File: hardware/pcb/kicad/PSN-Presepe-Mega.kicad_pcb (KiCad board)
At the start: 2 copper layers, 280 x 170 mm, 83 parts, among them J1 12V_IN, K1 G5Q-1_DC12, K10 G5Q-1_DC12, K11 G5Q-1_DC12, K12 G5Q-1_DC12, K13 G5Q-1_DC12, K14 G5Q-1_DC12, K15 G5Q-1_DC12, K16 G5Q-1_DC12, K2 G5Q-1_DC12, K3 G5Q-1_DC12, K4 G5Q-1_DC12, K5 G5Q-1_DC12, K6 G5Q-1_DC12, K7 G5Q-1_DC12, K8 G5Q-1_DC12, K9 G5Q-1_DC12, Q1 IRLZ44N_CIELO_R, Q2 IRLZ44N_CIELO_G, Q3 IRLZ44N_CIELO_B, Q4 IRLZ44N_TRAM_R, Q5 IRLZ44N_TRAM_G, Q6 IRLZ44N_TRAM_B, Q7 IRLZ44N_ALBA_R, Q8 IRLZ44N_ALBA_G, Q9 IRLZ44N_ALBA_B, U1 ULN2803C, U2 ULN2803C

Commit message: Promote KiCad-validated K4 coil route
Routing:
- net RELAY4_COIL_LOW: track 0.00 -> 76.4 mm
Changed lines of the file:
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@@
   (segment (start 191 69) (end 193.62 64) (width 0.3) (layer "F.Cu") (net 38))
   (segment (start 193.62 64) (end 193.62 60) (width 0.3) (layer "F.Cu") (net 38))
+  (segment (start 145.16 69.62) (end 148.0 71.5) (width 0.3) (layer "F.Cu") (net 39))
+  (segment (start 148.0 71.5) (end 209.0 71.5) (width 0.3) (layer "F.Cu") (net 39))
+  (segment (start 209.0 71.5) (end 211.62 64.0) (width 0.3) (layer "F.Cu") (net 39))
+  (segment (start 211.62 64.0) (end 211.62 60.0) (width 0.3) (layer "F.Cu") (net 39))
   (gr_rect (start 20 20) (end 300 190) (stroke (width 0.5) (type default)) (fill none) (layer "Edge.Cuts"))
   (gr_rect (start 53 128) (end 118 172) (stroke (width 0.3) (type dash)) (fill none) (layer "Dwgs.User"))

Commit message: Promote KiCad-validated K5 coil route
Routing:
- net RELAY5_COIL_LOW: track 0.00 -> 96.7 mm
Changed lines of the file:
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@@
   (segment (start 209.0 71.5) (end 211.62 64.0) (width 0.3) (layer "F.Cu") (net 39))
   (segment (start 211.62 64.0) (end 211.62 60.0) (width 0.3) (layer "F.Cu") (net 39))
+  (segment (start 145.16 72.16) (end 148 74) (width 0.3) (layer "F.Cu") (net 40))
+  (segment (start 148 74) (end 227 74) (width 0.3) (layer "F.Cu") (net 40))
+  (segment (start 227 74) (end 229.62 64) (width 0.3) (layer "F.Cu") (net 40))
+  (segment (start 229.62 64) (end 229.62 60) (width 0.3) (layer "F.Cu") (net 40))
   (gr_rect (start 20 20) (end 300 190) (stroke (width 0.5) (type default)) (fill none) (layer "Edge.Cuts"))
   (gr_rect (start 53 128) (end 118 172) (stroke (width 0.3) (type dash)) (fill none) (layer "Dwgs.User"))

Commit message: Promote KiCad-validated K6 coil route
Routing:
- net RELAY6_COIL_LOW: track 0.00 -> 117.1 mm
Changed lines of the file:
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@@
   (segment (start 227 74) (end 229.62 64) (width 0.3) (layer "F.Cu") (net 40))
   (segment (start 229.62 64) (end 229.62 60) (width 0.3) (layer "F.Cu") (net 40))
+  (segment (start 145.16 74.7) (end 148 76.5) (width 0.3) (layer "F.Cu") (net 41))
+  (segment (start 148 76.5) (end 245 76.5) (width 0.3) (layer "F.Cu") (net 41))
+  (segment (start 245 76.5) (end 247.62 64) (width 0.3) (layer "F.Cu") (net 41))
+  (segment (start 247.62 64) (end 247.62 60) (width 0.3) (layer "F.Cu") (net 41))
   (gr_rect (start 20 20) (end 300 190) (stroke (width 0.5) (type default)) (fill none) (layer "Edge.Cuts"))
   (gr_rect (start 53 128) (end 118 172) (stroke (width 0.3) (type dash)) (fill none) (layer "Dwgs.User"))

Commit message: Promote KiCad-validated K7 coil route
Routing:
- net RELAY7_COIL_LOW: track 0.00 -> 137.6 mm
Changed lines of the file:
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@@
   (segment (start 245 76.5) (end 247.62 64) (width 0.3) (layer "F.Cu") (net 41))
   (segment (start 247.62 64) (end 247.62 60) (width 0.3) (layer "F.Cu") (net 41))
+  (segment (start 145.16 77.24) (end 148 79) (width 0.3) (layer "F.Cu") (net 42))
+  (segment (start 148 79) (end 263 79) (width 0.3) (layer "F.Cu") (net 42))
+  (segment (start 263 79) (end 265.62 64) (width 0.3) (layer "F.Cu") (net 42))
+  (segment (start 265.62 64) (end 265.62 60) (width 0.3) (layer "F.Cu") (net 42))
   (gr_rect (start 20 20) (end 300 190) (stroke (width 0.5) (type default)) (fill none) (layer "Edge.Cuts"))
   (gr_rect (start 53 128) (end 118 172) (stroke (width 0.3) (type dash)) (fill none) (layer "Dwgs.User"))

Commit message: Promote KiCad-validated K8 coil route
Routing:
- net RELAY8_COIL_LOW: track 0.00 -> 158.0 mm
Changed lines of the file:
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@@
   (segment (start 263 79) (end 265.62 64) (width 0.3) (layer "F.Cu") (net 42))
   (segment (start 265.62 64) (end 265.62 60) (width 0.3) (layer "F.Cu") (net 42))
+  (segment (start 145.16 79.78) (end 148 81.5) (width 0.3) (layer "F.Cu") (net 43))
+  (segment (start 148 81.5) (end 281 81.5) (width 0.3) (layer "F.Cu") (net 43))
+  (segment (start 281 81.5) (end 283.62 64) (width 0.3) (layer "F.Cu") (net 43))
+  (segment (start 283.62 64) (end 283.62 60) (width 0.3) (layer "F.Cu") (net 43))
   (gr_rect (start 20 20) (end 300 190) (stroke (width 0.5) (type default)) (fill none) (layer "Edge.Cuts"))
   (gr_rect (start 53 128) (end 118 172) (stroke (width 0.3) (type dash)) (fill none) (layer "Dwgs.User"))

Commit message: Promote KiCad-validated K9 coil route
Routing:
- net RELAY9_COIL_LOW: track 0.00 -> 34.2 mm
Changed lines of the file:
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@@
   (segment (start 281 81.5) (end 283.62 64) (width 0.3) (layer "F.Cu") (net 43))
   (segment (start 283.62 64) (end 283.62 60) (width 0.3) (layer "F.Cu") (net 43))
+  (segment (start 145.16 92) (end 147.5 94) (width 0.3) (layer "F.Cu") (net 44))
+  (segment (start 147.5 94) (end 147.5 112) (width 0.3) (layer "F.Cu") (net 44))
+  (segment (start 147.5 112) (end 157.62 112) (width 0.3) (layer "F.Cu") (net 44))
+  (segment (start 157.62 112) (end 157.62 115) (width 0.3) (layer "F.Cu") (net 44))
   (gr_rect (start 20 20) (end 300 190) (stroke (width 0.5) (type default)) (fill none) (layer "Edge.Cuts"))
   (gr_rect (start 53 128) (end 118 172) (stroke (width 0.3) (type dash)) (fill none) (layer "Dwgs.User"))

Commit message: Promote KiCad-validated K10 coil route
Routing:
- net RELAY10_COIL_LOW: track 0.00 -> 61.8 mm
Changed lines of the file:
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@@
   (segment (start 147.5 112) (end 157.62 112) (width 0.3) (layer "F.Cu") (net 44))
   (segment (start 157.62 112) (end 157.62 115) (width 0.3) (layer "F.Cu") (net 44))
+  (segment (start 145.16 94.54) (end 142 96.5) (width 0.3) (layer "F.Cu") (net 45))
+  (segment (start 142 96.5) (end 142 118) (width 0.3) (layer "F.Cu") (net 45))
+  (segment (start 142 118) (end 175.62 118) (width 0.3) (layer "F.Cu") (net 45))
+  (segment (start 175.62 118) (end 175.62 115) (width 0.3) (layer "F.Cu") (net 45))
   (gr_rect (start 20 20) (end 300 190) (stroke (width 0.5) (type default)) (fill none) (layer "Edge.Cuts"))
   (gr_rect (start 53 128) (end 118 172) (stroke (width 0.3) (type dash)) (fill none) (layer "Dwgs.User"))

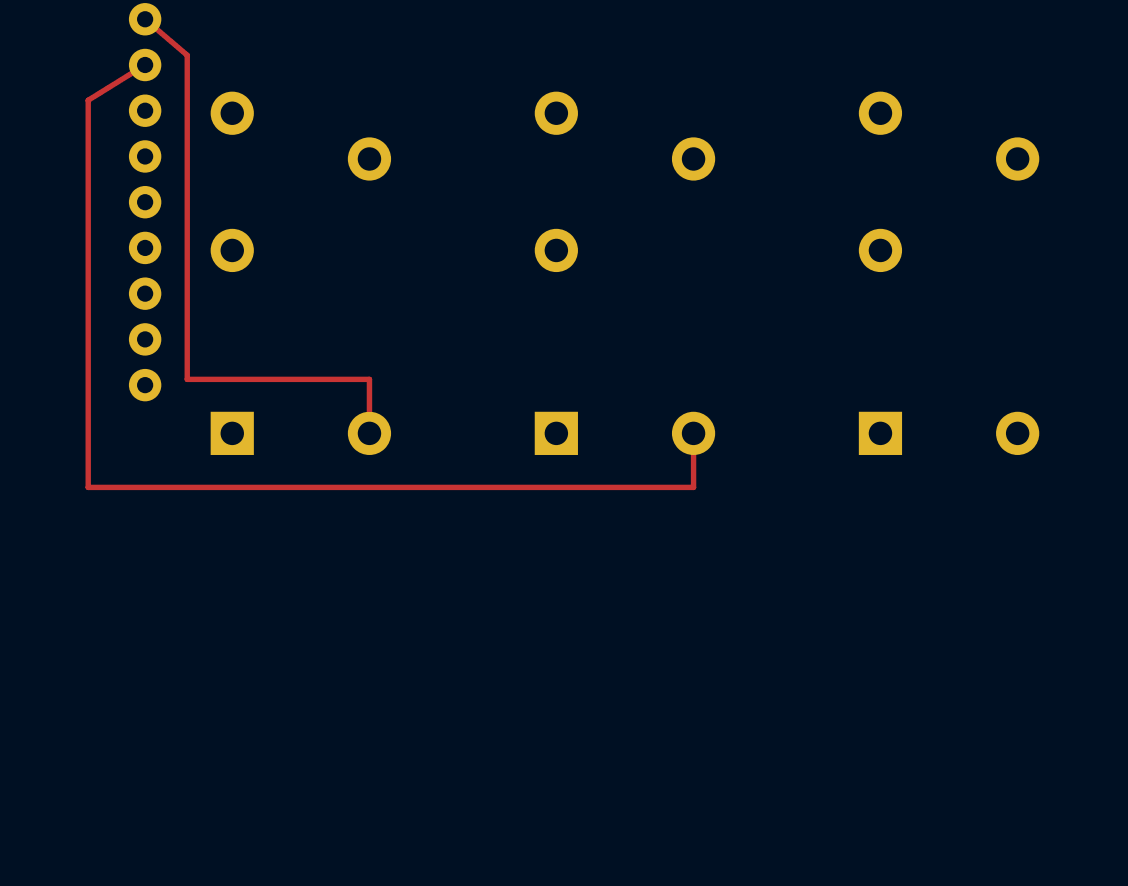
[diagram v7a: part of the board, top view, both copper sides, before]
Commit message: Promote KiCad-validated K11 coil route
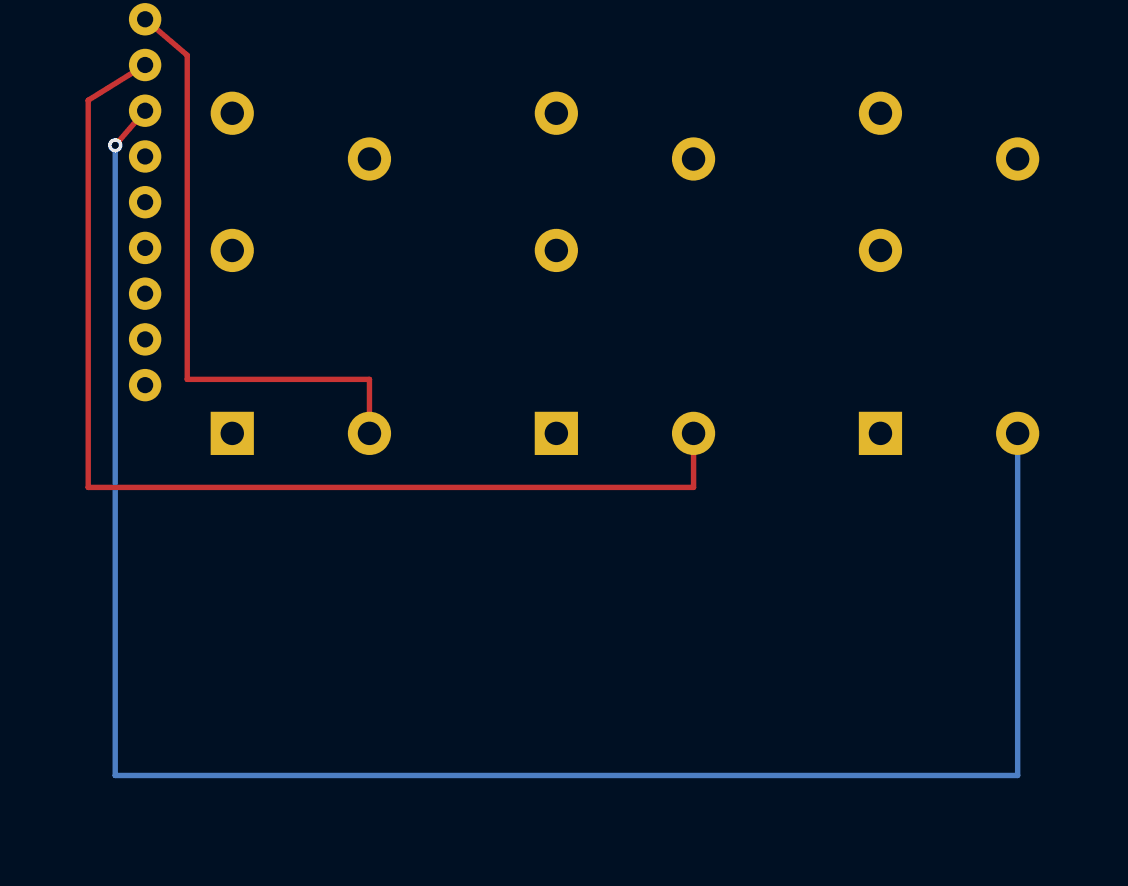
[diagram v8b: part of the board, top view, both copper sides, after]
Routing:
- net RELAY11_COIL_LOW: track 0.00 -> 106.7 mm, vias 0 -> 1
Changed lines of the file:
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@@
   (segment (start 142 118) (end 175.62 118) (width 0.3) (layer "F.Cu") (net 45))
   (segment (start 175.62 118) (end 175.62 115) (width 0.3) (layer "F.Cu") (net 45))
+  (segment (start 145.16 97.08) (end 143.5 99.0) (width 0.3) (layer "F.Cu") (net 46))
+  (via (at 143.5 99.0) (size 0.8) (drill 0.4) (layers "F.Cu" "B.Cu") (net 46))
+  (segment (start 143.5 99.0) (end 143.5 134.0) (width 0.3) (layer "B.Cu") (net 46))
+  (segment (start 143.5 134.0) (end 193.62 134.0) (width 0.3) (layer "B.Cu") (net 46))
+  (segment (start 193.62 134.0) (end 193.62 115.0) (width 0.3) (layer "B.Cu") (net 46))
   (gr_rect (start 20 20) (end 300 190) (stroke (width 0.5) (type default)) (fill none) (layer "Edge.Cuts"))
   (gr_rect (start 53 128) (end 118 172) (stroke (width 0.3) (type dash)) (fill none) (layer "Dwgs.User"))
